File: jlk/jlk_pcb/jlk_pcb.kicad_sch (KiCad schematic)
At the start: 48 parts, among them SW0 SWITCH_PUSH, SW1 SWITCH_PUSH, SW10 SWITCH_PUSH, SW11 SWITCH_PUSH, SW12 SWITCH_PUSH, SW13 SWITCH_PUSH, SW14 SWITCH_PUSH, SW15 SWITCH_PUSH, SW16 SWITCH_PUSH, SW17 SWITCH_PUSH, SW18 SWITCH_PUSH, SW19 SWITCH_PUSH, SW2 SWITCH_PUSH, SW20 SWITCH_PUSH, SW21 SWITCH_PUSH, SW22 SWITCH_PUSH, SW23 SWITCH_PUSH, SW24 SWITCH_PUSH, SW25 SWITCH_PUSH, SW26 SWITCH_PUSH, SW27 SWITCH_PUSH, SW28 SWITCH_PUSH, SW29 SWITCH_PUSH, SW3 SWITCH_PUSH, SW30 SWITCH_PUSH, SW31 SWITCH_PUSH, SW32 SWITCH_PUSH, SW33 SWITCH_PUSH, SW4 SWITCH_PUSH, SW5 SWITCH_PUSH, SW6 SWITCH_PUSH, SW7 SWITCH_PUSH, SW8 SWITCH_PUSH, SW9 SWITCH_PUSH, U0 ARDUINO_PRO_MICRO, U1 RESET_BUTTON

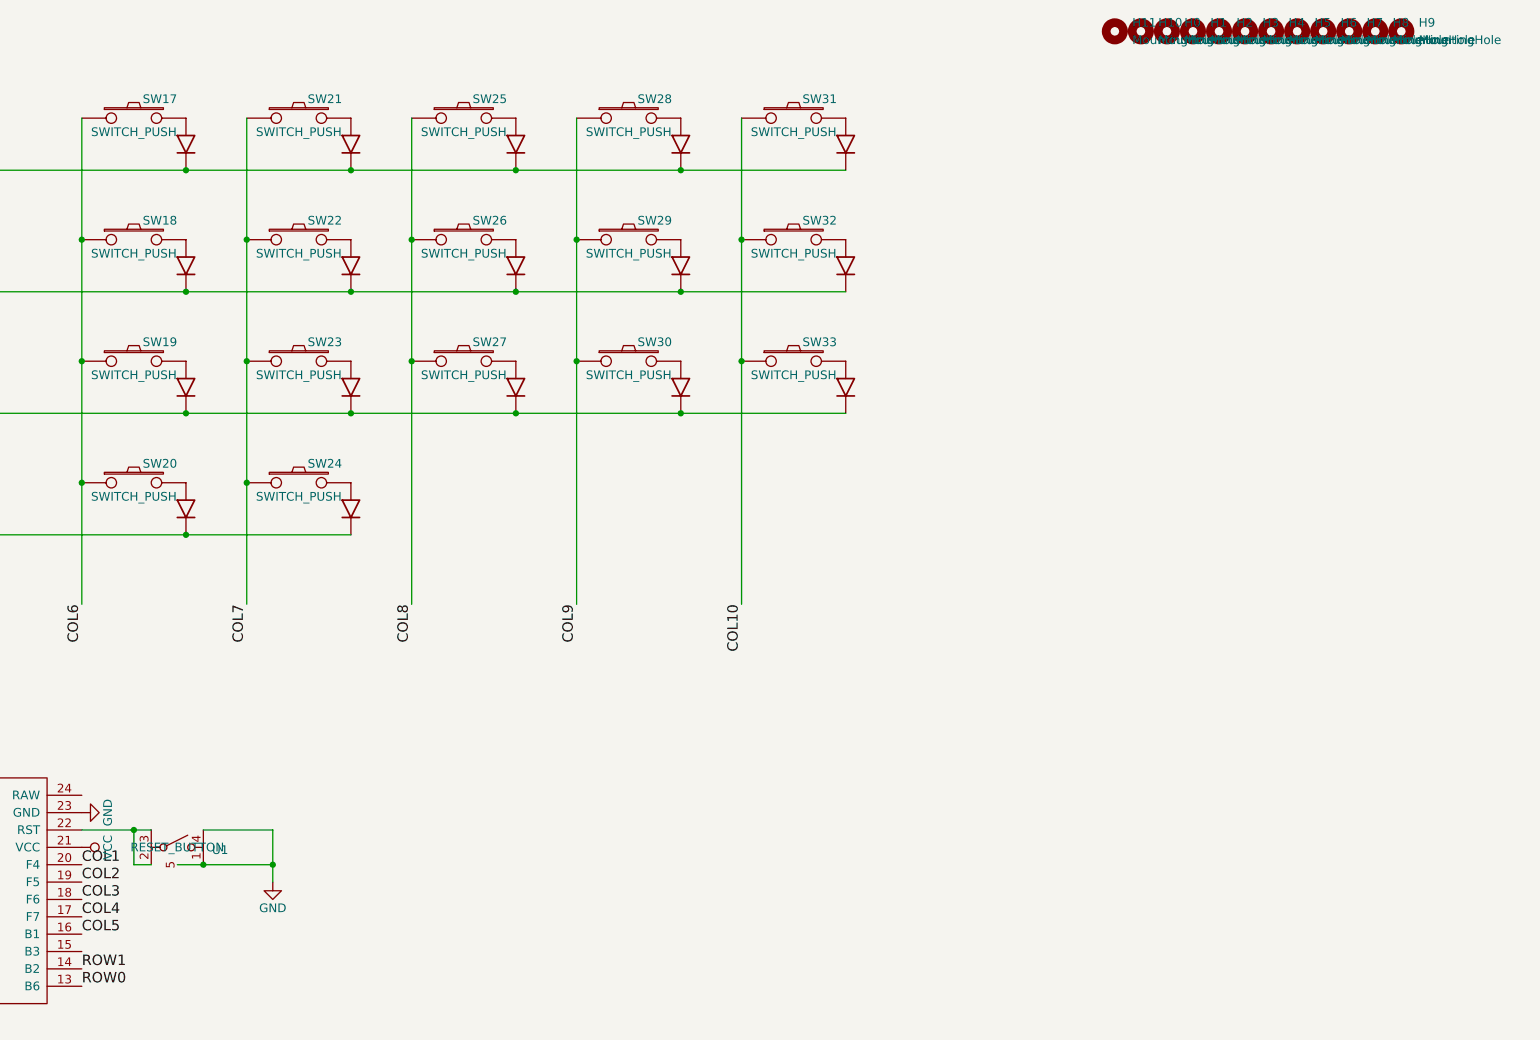
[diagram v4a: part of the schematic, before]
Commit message: Changed reset button again. Removed some standoffs.
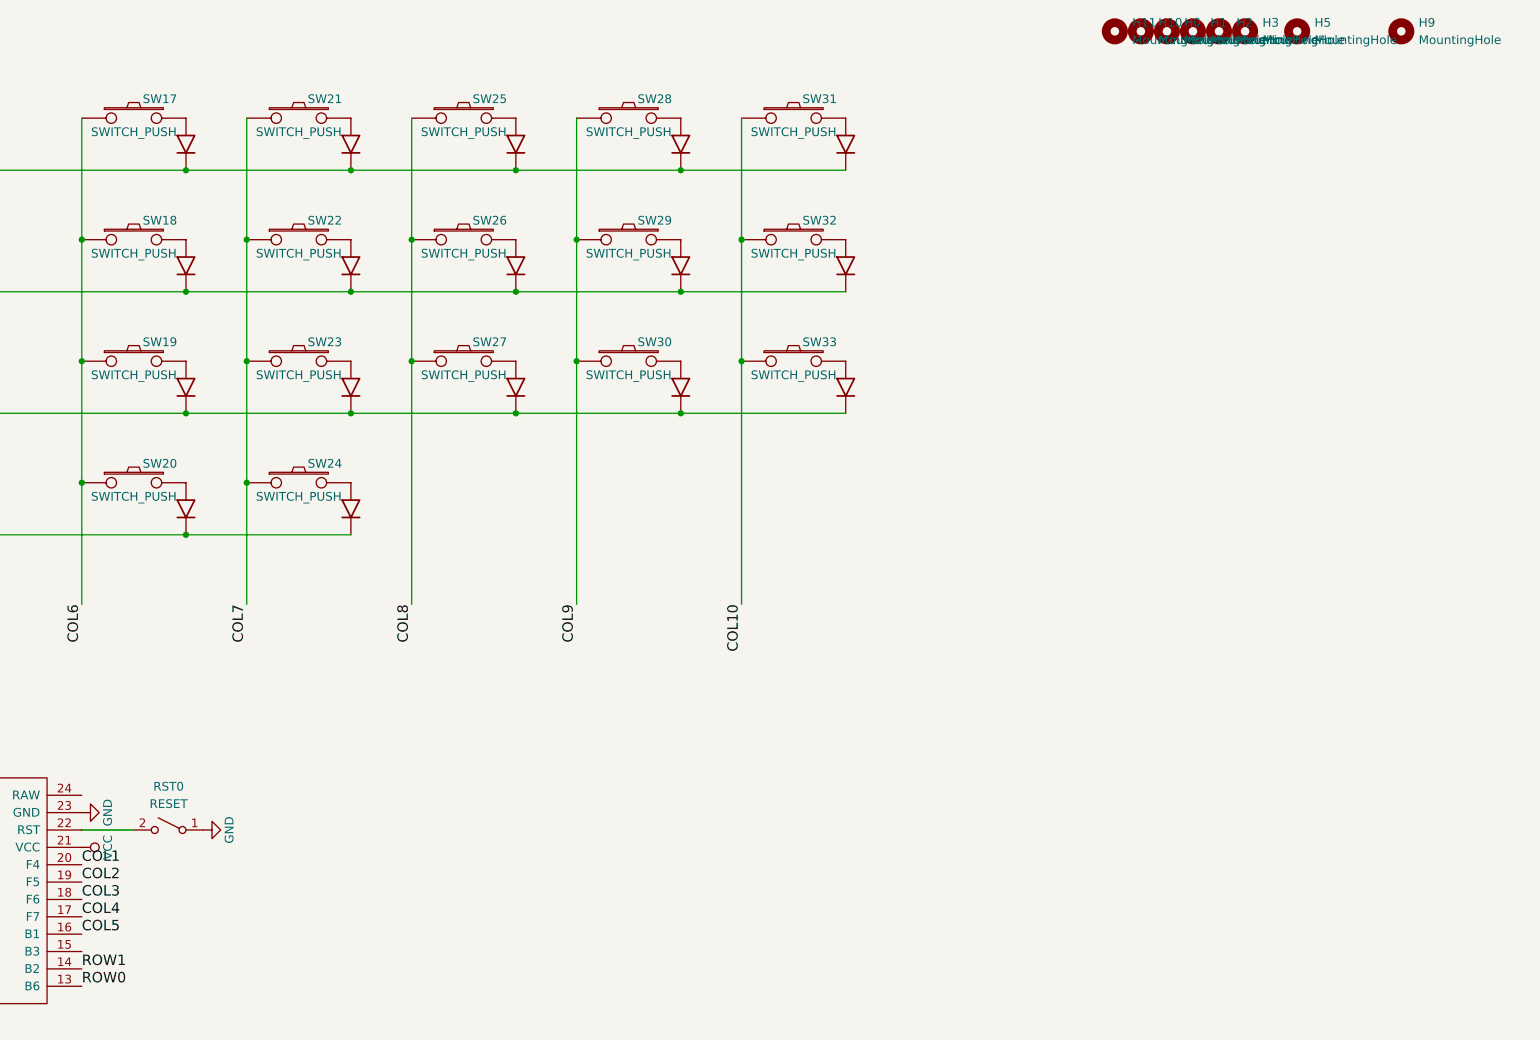
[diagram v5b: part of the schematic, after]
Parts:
- removed H4, H6, H7, H8: MountingHole, MountingHole:MountingHole_3.5mm, symbol Mechanical:MountingHole
- removed U1: RESET_BUTTON, footprints:reset_button_1, symbol symbols:RESET_BUTTON
- added RST0: RESET, footprints:reset_button_1, symbol Switch:SW_SPST
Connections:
- net GND: now also RST0.1 (A)
- net at U0.22 (RST): now also RST0.2 (B)
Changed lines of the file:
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@@
 (kicad_sch (version 20230121) (generator eeschema)
   (paper "USLedger")
-  (junction (at 226.06 154.94) (diameter 0) (color 0 0 0 0)
-  )
   (junction (at 294.64 63.5) (diameter 0) (color 0 0 0 0)
   )
@@
   (junction (at 285.75 71.12) (diameter 0) (color 0 0 0 0)
   )
-  (junction (at 205.74 149.86) (diameter 0) (color 0 0 0 0)
-  )
   (junction (at 53.34 81.28) (diameter 0) (color 0 0 0 0)
   )
-  (junction (at 215.9 154.94) (diameter 0) (color 0 0 0 0)
-  )
   (junction (at 149.86 63.5) (diameter 0) (color 0 0 0 0)
   )
@@
     (stroke (width 0) (type default))
   )
-  (wire (pts (xy 215.9 154.94) (xy 226.06 154.94))
-    (stroke (width 0) (type default))
-  )
   (wire (pts (xy 92.71 88.9) (xy 116.84 88.9))
     (stroke (width 0) (type default))
@@
     (stroke (width 0) (type default))
   )
-  (wire (pts (xy 226.06 149.86) (xy 226.06 154.94))
-    (stroke (width 0) (type default))
-  )
   (wire (pts (xy 237.49 71.12) (xy 261.62 71.12))
     (stroke (width 0) (type default))
@@
     (stroke (width 0) (type default))
   )
-  (wire (pts (xy 215.9 149.86) (xy 226.06 149.86))
-    (stroke (width 0) (type default))
-  )
   (wire (pts (xy 222.25 63.5) (xy 222.25 81.28))
     (stroke (width 0) (type default))
   )
-  (wire (pts (xy 212.09 154.94) (xy 215.9 154.94))
-    (stroke (width 0) (type default))
-  )
   (wire (pts (xy 92.71 71.12) (xy 116.84 71.12))
     (stroke (width 0) (type default))
   )
-  (wire (pts (xy 208.28 154.94) (xy 205.74 154.94))
-    (stroke (width 0) (type default))
-  )
   (wire (pts (xy 77.47 81.28) (xy 77.47 116.84))
     (stroke (width 0) (type default))
@@
     (stroke (width 0) (type default))
   )
-  (wire (pts (xy 205.74 149.86) (xy 208.28 149.86))
-    (stroke (width 0) (type default))
-  )
   (wire (pts (xy 101.6 63.5) (xy 101.6 81.28))
     (stroke (width 0) (type default))
   )
-  (wire (pts (xy 205.74 154.94) (xy 205.74 149.86))
-    (stroke (width 0) (type default))
-  )
   (wire (pts (xy 270.51 81.28) (xy 270.51 116.84))
     (stroke (width 0) (type default))
@@
   )
   (wire (pts (xy 125.73 45.72) (xy 125.73 63.5))
-    (stroke (width 0) (type default))
-  )
-  (wire (pts (xy 226.06 154.94) (xy 226.06 157.48))
     (stroke (width 0) (type default))
   )
@@
     )
   )
-  (symbol (lib_id "Atreus62-rescue:GND") (at 226.06 157.48 0) (unit 1)
-    (in_bom yes) (on_board yes) (dnp no)
-    (property "Reference" "#PWR04" (at 226.06 163.83 0)
-      (effects (font (size 1.27 1.27)) hide)
-    )
-    (property "Value" "GND" (at 226.06 161.29 0)
-      (effects (font (size 1.27 1.27)))
-    )
-    (property "Footprint" "" (at 226.06 157.48 0)
-      (effects (font (size 1.27 1.27)))
-    )
-    (property "Datasheet" "" (at 226.06 157.48 0)
+  (symbol (lib_id "Atreus62-rescue:GND") (at 215.9 149.86 90) (unit 1)
+    (in_bom yes) (on_board yes) (dnp no)
+    (property "Reference" "#PWR04" (at 222.25 149.86 0)
+      (effects (font (size 1.27 1.27)) hide)
+    )
+    (property "Value" "GND" (at 219.71 149.86 0)
+      (effects (font (size 1.27 1.27)))
+    )
+    (property "Footprint" "" (at 215.9 149.86 0)
+      (effects (font (size 1.27 1.27)))
+    )
+    (property "Datasheet" "" (at 215.9 149.86 0)
       (effects (font (size 1.27 1.27)))
     )
@@
     )
   )
-  (symbol (lib_id "Mechanical:MountingHole") (at 387.35 33.02 0) (unit 1)
-    (in_bom yes) (on_board yes) (dnp no) (fields_autoplaced)
-    (property "Reference" "H8" (at 389.89 31.75 0)
-      (effects (font (size 1.27 1.27)) (justify left))
-    )
-    (property "Value" "MountingHole" (at 389.89 34.29 0)
-      (effects (font (size 1.27 1.27)) (justify left))
-    )
-    (property "Footprint" "MountingHole:MountingHole_3.5mm" (at 387.35 33.02 0)
-      (effects (font (size 1.27 1.27)) hide)
-    )
-    (property "Datasheet" "~" (at 387.35 33.02 0)
-      (effects (font (size 1.27 1.27)) hide)
-    )
-    (instances
-      (project "jlk_pcb"
-        (path "/97127b28-60f4-45ff-835e-dccfbc833331"
-          (reference "H8") (unit 1)
-        )
-      )
-    )
-  )
   (symbol (lib_id "Mechanical:MountingHole") (at 391.16 33.02 0) (unit 1)
     (in_bom yes) (on_board yes) (dnp no) (fields_autoplaced)
@@
     )
   )
-  (symbol (lib_id "symbols:RESET_BUTTON") (at 212.09 152.4 270) (unit 1)
-    (in_bom yes) (on_board yes) (dnp no) (fields_autoplaced)
-    (property "Reference" "U1" (at 217.17 152.781 90)
-      (effects (font (size 1.27 1.27)) (justify left))
-    )
-    (property "Value" "RESET_BUTTON" (at 212.09 152.4 90)
-      (effects (font (size 1.27 1.27)))
-    )
-    (property "Footprint" "footprints:reset_button_1" (at 212.09 152.4 90)
-      (effects (font (size 1.27 1.27)) hide)
-    )
-    (property "Datasheet" "" (at 212.09 152.4 90)
-      (effects (font (size 1.27 1.27)) hide)
-    )
-    (pin "2")
-    (pin "3")
-    (pin "4")
-    (pin "5")
-    (pin "1")
-    (instances
-      (project "jlk_pcb"
-        (path "/97127b28-60f4-45ff-835e-dccfbc833331"
-          (reference "U1") (unit 1)
-        )
-      )
-    )
-  )
-  (symbol (lib_id "Mechanical:MountingHole") (at 379.73 33.02 0) (unit 1)
-    (in_bom yes) (on_board yes) (dnp no) (fields_autoplaced)
-    (property "Reference" "H6" (at 382.27 31.75 0)
-      (effects (font (size 1.27 1.27)) (justify left))
-    )
-    (property "Value" "MountingHole" (at 382.27 34.29 0)
-      (effects (font (size 1.27 1.27)) (justify left))
-    )
-    (property "Footprint" "MountingHole:MountingHole_3.5mm" (at 379.73 33.02 0)
-      (effects (font (size 1.27 1.27)) hide)
-    )
-    (property "Datasheet" "~" (at 379.73 33.02 0)
-      (effects (font (size 1.27 1.27)) hide)
-    )
-    (instances
-      (project "jlk_pcb"
-        (path "/97127b28-60f4-45ff-835e-dccfbc833331"
-          (reference "H6") (unit 1)
-        )
-      )
-    )
-  )
   (symbol (lib_id "Mechanical:MountingHole") (at 364.49 33.02 0) (unit 1)
     (in_bom yes) (on_board yes) (dnp no) (fields_autoplaced)
@@
     )
   )
-  (symbol (lib_id "Mechanical:MountingHole") (at 372.11 33.02 0) (unit 1)
-    (in_bom yes) (on_board yes) (dnp no) (fields_autoplaced)
-    (property "Reference" "H4" (at 374.65 31.75 0)
-      (effects (font (size 1.27 1.27)) (justify left))
-    )
-    (property "Value" "MountingHole" (at 374.65 34.29 0)
-      (effects (font (size 1.27 1.27)) (justify left))
-    )
-    (property "Footprint" "MountingHole:MountingHole_3.5mm" (at 372.11 33.02 0)
-      (effects (font (size 1.27 1.27)) hide)
-    )
-    (property "Datasheet" "~" (at 372.11 33.02 0)
-      (effects (font (size 1.27 1.27)) hide)
-    )
-    (instances
-      (project "jlk_pcb"
-        (path "/97127b28-60f4-45ff-835e-dccfbc833331"
-          (reference "H4") (unit 1)
-        )
-      )
-    )
-  )
   (symbol (lib_id "Mechanical:MountingHole") (at 368.3 33.02 0) (unit 1)
     (in_bom yes) (on_board yes) (dnp no) (fields_autoplaced)
@@
     )
   )
-  (symbol (lib_id "Mechanical:MountingHole") (at 383.54 33.02 0) (unit 1)
-    (in_bom yes) (on_board yes) (dnp no) (fields_autoplaced)
-    (property "Reference" "H7" (at 386.08 31.75 0)
-      (effects (font (size 1.27 1.27)) (justify left))
-    )
-    (property "Value" "MountingHole" (at 386.08 34.29 0)
-      (effects (font (size 1.27 1.27)) (justify left))
-    )
-    (property "Footprint" "MountingHole:MountingHole_3.5mm" (at 383.54 33.02 0)
-      (effects (font (size 1.27 1.27)) hide)
-    )
-    (property "Datasheet" "~" (at 383.54 33.02 0)
-      (effects (font (size 1.27 1.27)) hide)
-    )
-    (instances
-      (project "jlk_pcb"
-        (path "/97127b28-60f4-45ff-835e-dccfbc833331"
-          (reference "H7") (unit 1)
-        )
-      )
+  (symbol (lib_id "Switch:SW_SPST") (at 210.82 149.86 0) (mirror y) (unit 1)
+    (in_bom yes) (on_board yes) (dnp no)
+    (property "Reference" "RST0" (at 210.82 143.51 0)
+      (effects (font (size 1.27 1.27)))
+    )
+    (property "Value" "RESET" (at 210.82 146.05 0)
+      (effects (font (size 1.27 1.27)))
+    )
+    (property "Footprint" "footprints:reset_button_1" (at 210.82 149.86 0)
+      (effects (font (size 1.27 1.27)) hide)
+    )
+    (property "Datasheet" "~" (at 210.82 149.86 0)
+      (effects (font (size 1.27 1.27)) hide)
+    )
+    (pin "1")
+    (pin "2")
+    (instances
+      (project "jlk_pcb"
+        (path "/97127b28-60f4-45ff-835e-dccfbc833331"
+          (reference "RST0") (unit 1)
+        )
+      )
